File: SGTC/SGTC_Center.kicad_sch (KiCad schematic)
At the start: 0 parts

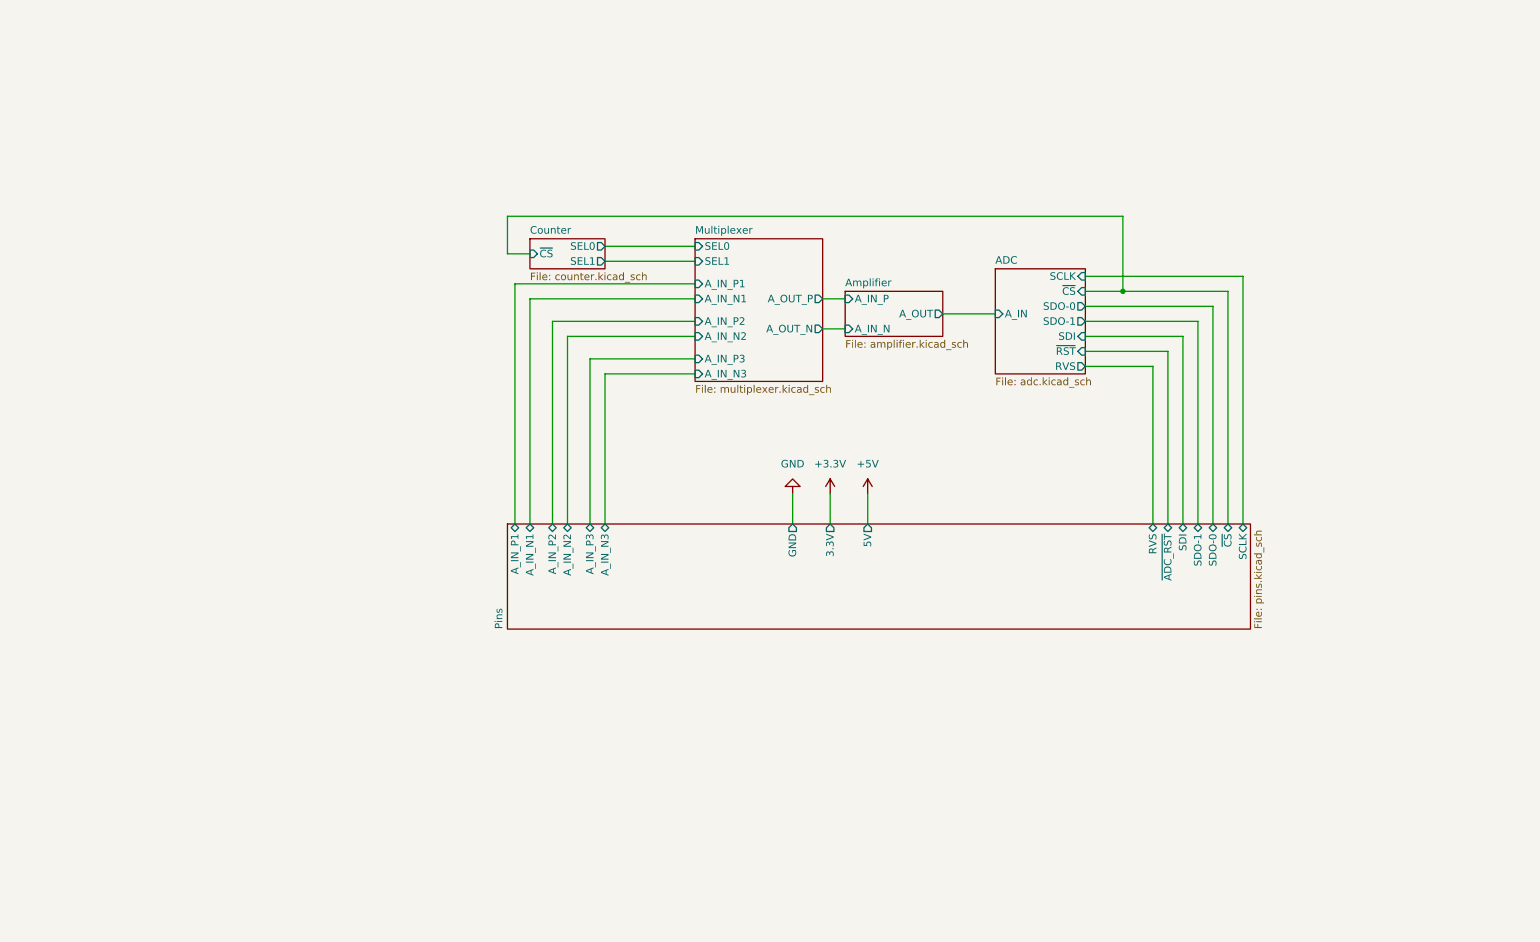
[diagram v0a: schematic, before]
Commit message: redo schematic for fin board
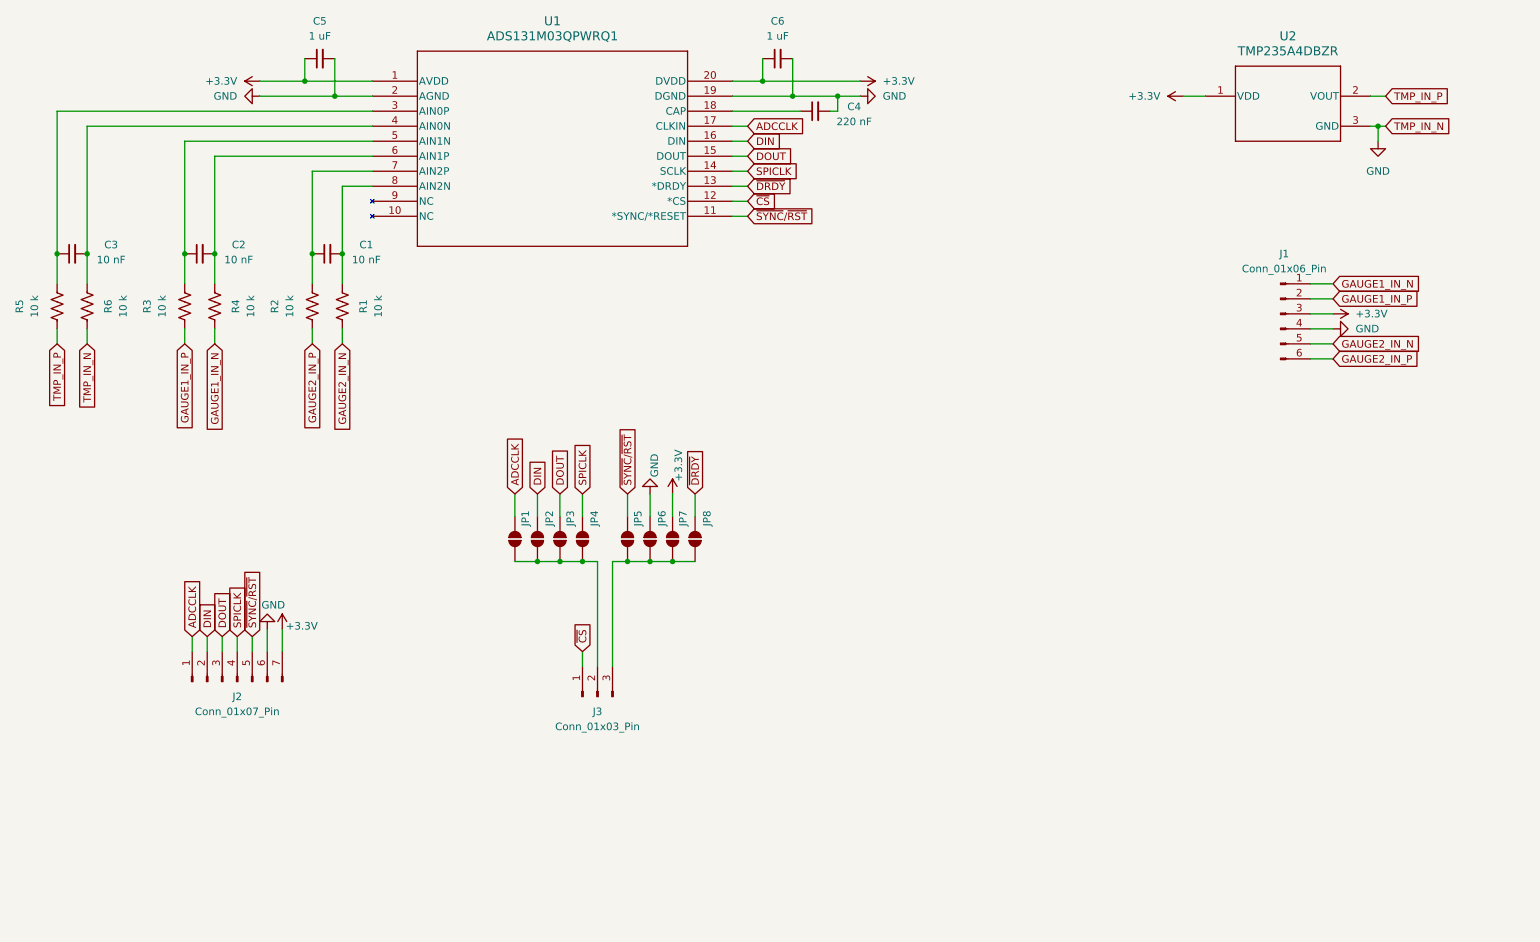
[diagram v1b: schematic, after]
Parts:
- added C1, C2, C3: 10 nF, symbol Device:C_Small
- added C4: 220 nF, symbol Device:C_Small
- added C5, C6: 1 uF, symbol Device:C_Small
- added J1: Conn_01x06_Pin, symbol Connector:Conn_01x06_Pin
- added J2: Conn_01x07_Pin, symbol Connector:Conn_01x07_Pin
- added J3: Conn_01x03_Pin, symbol Connector:Conn_01x03_Pin
- added JP1, JP2, JP3, JP4, JP5, JP6, JP7, JP8: SolderJumper_2_Open, symbol Jumper:SolderJumper_2_Open
- added R1, R2, R3, R4, R5, R6: 10 k, symbol Device:R_US
- added U1: ADS131M03QPWRQ1, TSSOP20_PW_TEX, symbol FinLib:ADS131M03QPWRQ1
- added U2: TMP235A4DBZR, DBZ0003A-IPC_A, symbol FinLib:TMP235A4DBZR
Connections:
- net +3.3V: now also C5.1, C6.1, J1.3 (Pin_3), J2.7 (Pin_7), JP7.2 (B), U1.1 (AVDD), U1.20 (DVDD), U2.1 (VDD)
- net GND: now also C4.2, C5.2, C6.2, J1.4 (Pin_4), J2.6 (Pin_6), JP6.2 (B), R6.2, U1.19 (DGND), U1.2 (AGND), U2.3 (GND)
- new net: J3.2 (Pin_2), JP1.1 (A), JP2.1 (A), JP3.1 (A), JP4.1 (A)
- new net: C1.1, R2.2, U1.7 (AIN2P)
- new net: C1.2, R1.1, U1.8 (AIN2N)
- new net: C3.1, R5.2, U1.3 (AIN0P)
- new net: C3.2, R6.1, U1.4 (AIN0N)
- new net: C2.1, R3.2, U1.5 (AIN1N)
- new net: C2.2, R4.1, U1.6 (AIN1P)
- new net: J3.3 (Pin_3), JP5.1 (A), JP6.1 (A), JP7.1 (A), JP8.1 (A)
- new net: C4.1, U1.18 (CAP)
- new net ADCCLK: J2.1 (Pin_1), JP1.2 (B), U1.17 (CLKIN)
- new net DIN: J2.2 (Pin_2), JP2.2 (B), U1.16 (DIN)
- new net DOUT: J2.3 (Pin_3), JP3.2 (B), U1.15 (DOUT)
- new net GAUGE1_IN_N: J1.1 (Pin_1), R4.2
- new net GAUGE1_IN_P: J1.2 (Pin_2), R3.1
- new net GAUGE2_IN_N: J1.5 (Pin_5), R1.2
- new net GAUGE2_IN_P: J1.6 (Pin_6), R2.1
- new net SPICLK: J2.4 (Pin_4), JP4.2 (B), U1.14 (SCLK)
- new net TMP_IN_P: R5.1, U2.2 (VOUT)
- new net ~{CS}: J3.1 (Pin_1), U1.12 (*CS)
- new net ~{DRDY}: JP8.2 (B), U1.13 (*DRDY)
- new net ~{SYNC}/~{RST}: J2.5 (Pin_5), JP5.2 (B), U1.11 (*SYNC/*RESET)
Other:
- removed sheet ADC
- removed sheet Amplifier
- removed sheet Counter
- removed sheet Multiplexer
- removed sheet Pins

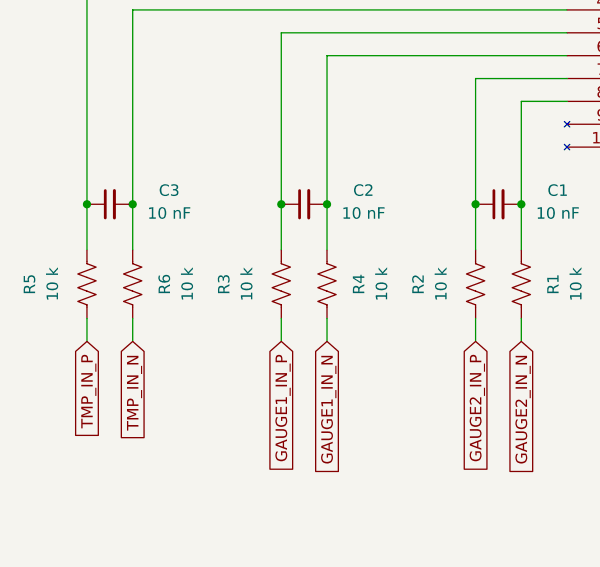
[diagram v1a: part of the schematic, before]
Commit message: fin center draft
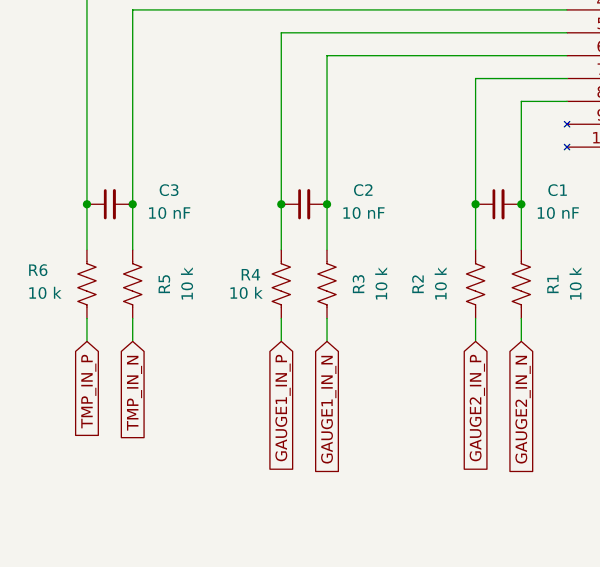
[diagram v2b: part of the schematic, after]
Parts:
- C1, C2, C3, C4, C5, C6: footprint (none) -> Capacitor_SMD:C_0603_1608Metric
- J1: footprint (none) -> Connector_PinHeader_2.54mm:PinHeader_1x06_P2.54mm_Vertical
- J2: footprint (none) -> Connector_PinHeader_2.54mm:PinHeader_1x07_P2.54mm_Vertical
- J3: footprint (none) -> Connector_PinHeader_2.54mm:PinHeader_1x03_P2.54mm_Vertical
- JP1, JP2, JP3, JP4, JP5, JP6, JP7, JP8: footprint (none) -> Jumper:SolderJumper-2_P1.3mm_Open_RoundedPad1.0x1.5mm
- R1, R2: footprint (none) -> Resistor_SMD:R_0603_1608Metric
- R3: renamed from R4; footprint (none) -> Resistor_SMD:R_0603_1608Metric
- R4: renamed from R3; footprint (none) -> Resistor_SMD:R_0603_1608Metric
- R5: renamed from R6; footprint (none) -> Resistor_SMD:R_0603_1608Metric
- R6: renamed from R5; footprint (none) -> Resistor_SMD:R_0603_1608Metric
- U1: footprint TSSOP20_PW_TEX -> FinLib:ADS131M03
- U2: footprint DBZ0003A-IPC_A -> FinLib:TMP235A4DBZR
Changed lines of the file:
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@@
 			)
 		)
-		(property "Footprint" ""
+		(property "Footprint" "Capacitor_SMD:C_0603_1608Metric"
 			(at 146.05 48.26 0)
 			(effects
@@
 			)
 		)
-		(property "Footprint" ""
+		(property "Footprint" "Jumper:SolderJumper-2_P1.3mm_Open_RoundedPad1.0x1.5mm"
 			(at 101.6 129.54 0)
 			(effects
@@
 			)
 		)
-		(property "Footprint" ""
+		(property "Footprint" "Jumper:SolderJumper-2_P1.3mm_Open_RoundedPad1.0x1.5mm"
 			(at 105.41 129.54 0)
 			(effects
@@
 			)
 		)
-		(property "Footprint" ""
+		(property "Footprint" "Jumper:SolderJumper-2_P1.3mm_Open_RoundedPad1.0x1.5mm"
 			(at 109.22 129.54 0)
 			(effects
@@
 			)
 		)
-		(property "Footprint" ""
+		(property "Footprint" "Capacitor_SMD:C_0603_1608Metric"
 			(at 69.85 81.28 0)
 			(effects
@@
 			)
 		)
-		(property "Footprint" ""
+		(property "Footprint" "Jumper:SolderJumper-2_P1.3mm_Open_RoundedPad1.0x1.5mm"
 			(at 113.03 129.54 0)
 			(effects
@@
 			)
 		)
-		(property "Footprint" ""
+		(property "Footprint" "Capacitor_SMD:C_0603_1608Metric"
 			(at 26.67 81.28 0)
 			(effects
@@
 			)
 		)
-		(property "Footprint" ""
+		(property "Footprint" "Capacitor_SMD:C_0603_1608Metric"
 			(at 48.26 81.28 0)
 			(effects
@@
 			)
 		)
-		(property "Footprint" "DBZ0003A-IPC_A"
+		(property "Footprint" "FinLib:TMP235A4DBZR"
 			(at 218.44 54.61 0)
 			(effects
@@
 			)
 		)
-		(property "Footprint" ""
+		(property "Footprint" "Connector_PinHeader_2.54mm:PinHeader_1x06_P2.54mm_Vertical"
 			(at 231.14 91.44 0)
 			(effects
@@
 			)
 		)
-		(property "Footprint" ""
+		(property "Footprint" "Resistor_SMD:R_0603_1608Metric"
 			(at 66.294 89.916 90)
 			(effects
@@
 		(on_board yes)
 		(dnp no)
-		(property "Reference" "R4"
+		(property "Reference" "R3"
 			(at 54.356 90.17 90)
 			(effects
@@
 			)
 		)
-		(property "Footprint" ""
+		(property "Footprint" "Resistor_SMD:R_0603_1608Metric"
 			(at 51.816 90.424 90)
 			(effects
@@
 			(project "SGTC_Center"
 				(path "/cbc99ef0-5fa7-4678-bd4c-c2c08fe588b6"
-					(reference "R4")
+					(reference "R3")
 					(unit 1)
 				)
@@
 		(on_board yes)
 		(dnp no)
-		(fields_autoplaced yes)
-		(property "Reference" "R3"
-			(at 39.37 90.17 90)
-			(effects
-				(font
-					(size 1.27 1.27)
-				)
+		(property "Reference" "R4"
+			(at 41.148 89.154 0)
+			(effects
+				(font
+					(size 1.27 1.27)
+				)
+				(justify right)
 			)
 		)
 		(property "Value" "10 k"
-			(at 41.91 90.17 90)
-			(effects
-				(font
-					(size 1.27 1.27)
-				)
-			)
-		)
-		(property "Footprint" ""
+			(at 39.878 91.186 0)
+			(effects
+				(font
+					(size 1.27 1.27)
+				)
+				(justify right)
+			)
+		)
+		(property "Footprint" "Resistor_SMD:R_0603_1608Metric"
 			(at 44.704 89.916 90)
 			(effects
@@
 			(project "SGTC_Center"
 				(path "/cbc99ef0-5fa7-4678-bd4c-c2c08fe588b6"
-					(reference "R3")
+					(reference "R4")
 					(unit 1)
 				)
@@
 			)
 		)
-		(property "Footprint" ""
+		(property "Footprint" "Capacitor_SMD:C_0603_1608Metric"
 			(at 68.58 48.26 0)
 			(effects
@@
 			)
 		)
-		(property "Footprint" ""
+		(property "Footprint" "Jumper:SolderJumper-2_P1.3mm_Open_RoundedPad1.0x1.5mm"
 			(at 128.27 129.54 0)
 			(effects
@@
 			)
 		)
-		(property "Footprint" ""
+		(property "Footprint" "Connector_PinHeader_2.54mm:PinHeader_1x03_P2.54mm_Vertical"
 			(at 115.57 156.21 0)
 			(effects
@@
 		(on_board yes)
 		(dnp no)
-		(property "Reference" "R6"
+		(property "Reference" "R5"
 			(at 32.766 90.17 90)
 			(effects
@@
 			)
 		)
-		(property "Footprint" ""
+		(property "Footprint" "Resistor_SMD:R_0603_1608Metric"
 			(at 30.226 90.424 90)
 			(effects
@@
 			(project "SGTC_Center"
 				(path "/cbc99ef0-5fa7-4678-bd4c-c2c08fe588b6"
-					(reference "R6")
+					(reference "R5")
 					(unit 1)
 				)
@@
 			)
 		)
-		(property "Footprint" ""
+		(property "Footprint" "Jumper:SolderJumper-2_P1.3mm_Open_RoundedPad1.0x1.5mm"
 			(at 132.08 129.54 0)
 			(effects
@@
 		(on_board yes)
 		(dnp no)
-		(fields_autoplaced yes)
-		(property "Reference" "R5"
-			(at 17.78 90.17 90)
-			(effects
-				(font
-					(size 1.27 1.27)
-				)
+		(property "Reference" "R6"
+			(at 17.526 88.646 0)
+			(effects
+				(font
+					(size 1.27 1.27)
+				)
+				(justify right)
 			)
 		)
 		(property "Value" "10 k"
-			(at 20.32 90.17 90)
-			(effects
-				(font
-					(size 1.27 1.27)
-				)
-			)
-		)
-		(property "Footprint" ""
+			(at 17.526 91.186 0)
+			(effects
+				(font
+					(size 1.27 1.27)
+				)
+				(justify right)
+			)
+		)
+		(property "Footprint" "Resistor_SMD:R_0603_1608Metric"
 			(at 23.114 89.916 90)
 			(effects
@@
 			(project "SGTC_Center"
 				(path "/cbc99ef0-5fa7-4678-bd4c-c2c08fe588b6"
-					(reference "R5")
+					(reference "R6")
 					(unit 1)
 				)
@@
 			)
 		)
-		(property "Footprint" ""
+		(property "Footprint" "Jumper:SolderJumper-2_P1.3mm_Open_RoundedPad1.0x1.5mm"
 			(at 120.65 129.54 0)
 			(effects
@@
 			)
 		)
-		(property "Footprint" ""
+		(property "Footprint" "Resistor_SMD:R_0603_1608Metric"
 			(at 73.406 90.424 90)
 			(effects
@@
 			)
 		)
-		(property "Footprint" "TSSOP20_PW_TEX"
+		(property "Footprint" "FinLib:ADS131M03"
 			(at 77.47 52.07 0)
 			(effects
@@
 			)
 		)
-		(property "Footprint" ""
+		(property "Footprint" "Connector_PinHeader_2.54mm:PinHeader_1x07_P2.54mm_Vertical"
 			(at 54.61 153.67 0)
 			(effects
@@
 			)
 		)
-		(property "Footprint" ""
+		(property "Footprint" "Capacitor_SMD:C_0603_1608Metric"
 			(at 152.4 57.15 0)
 			(effects
@@
 			)
 		)
-		(property "Footprint" ""
+		(property "Footprint" "Jumper:SolderJumper-2_P1.3mm_Open_RoundedPad1.0x1.5mm"
 			(at 124.46 129.54 0)
 			(effects

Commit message: silkscreen things mostly
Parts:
- C1, C2, C3, C4, C5, C6: footprint Capacitor_SMD:C_0603_1608Metric -> (none)
- J1: footprint Connector_PinHeader_2.54mm:PinHeader_1x06_P2.54mm_Vertical -> (none)
- J2: footprint Connector_PinHeader_2.54mm:PinHeader_1x07_P2.54mm_Vertical -> (none)
- J3: footprint Connector_PinHeader_2.54mm:PinHeader_1x03_P2.54mm_Vertical -> (none)
- JP1, JP2, JP3, JP4, JP5, JP6, JP7, JP8: footprint Jumper:SolderJumper-2_P1.3mm_Open_RoundedPad1.0x1.5mm -> (none)
- R1, R2: footprint Resistor_SMD:R_0603_1608Metric -> (none)
- R3: renamed from R4; footprint Resistor_SMD:R_0603_1608Metric -> (none)
- R4: renamed from R3; footprint Resistor_SMD:R_0603_1608Metric -> (none)
- R5: renamed from R6; footprint Resistor_SMD:R_0603_1608Metric -> (none)
- R6: renamed from R5; footprint Resistor_SMD:R_0603_1608Metric -> (none)
- U1: footprint FinLib:ADS131M03 -> TSSOP20_PW_TEX
- U2: footprint FinLib:TMP235A4DBZR -> DBZ0003A-IPC_A
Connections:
- net at JP1.1 (A), JP2.1 (A), JP3.1 (A)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: now also J3.3 (Pin_3); no longer J3.2 (Pin_2)
- net at JP5.1 (A), JP6.1 (A), JP7.1 (A)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: now also J3.2 (Pin_2); no longer J3.3 (Pin_3)
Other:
- moved on the sheet: JP1, JP2, JP3, JP4, JP5, JP6, JP7, JP8

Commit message: final version
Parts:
- removed J2: Conn_01x07_Pin, symbol Connector:Conn_01x07_Pin
- added J2, J4, J5, J6, J7, J8, J9: Conn_01x01_Pin, Connector_PinHeader_2.54mm:PinHeader_1x01_P2.54mm_Vertical, symbol Connector:Conn_01x01_Pin
- C1, C2, C3, C4, C5, C6: footprint (none) -> Capacitor_SMD:C_0603_1608Metric
- J1: footprint (none) -> Connector_PinHeader_2.54mm:PinHeader_1x06_P2.54mm_Vertical
- J3: footprint (none) -> Connector_PinHeader_2.54mm:PinHeader_1x03_P2.54mm_Vertical
- JP1, JP2, JP3, JP4, JP5, JP6, JP7, JP8: footprint (none) -> Jumper:SolderJumper-2_P1.3mm_Open_RoundedPad1.0x1.5mm
- R1, R2, R3, R4, R5, R6: footprint (none) -> Resistor_SMD:R_0603_1608Metric
- U1: footprint TSSOP20_PW_TEX -> FinLib:ADS131M03
- U2: footprint DBZ0003A-IPC_A -> FinLib:TMP235A4DBZR
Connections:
- net +3.3V: now also J9.1 (Pin_1)
- net ADCCLK: now also J2.1 (Pin_1)
- net DIN: now also J4.1 (Pin_1)
- net DOUT: now also J5.1 (Pin_1)
- net GND: now also J8.1 (Pin_1)
- net SPICLK: now also J6.1 (Pin_1)
- net ~{SYNC}/~{RST}: now also J7.1 (Pin_1)

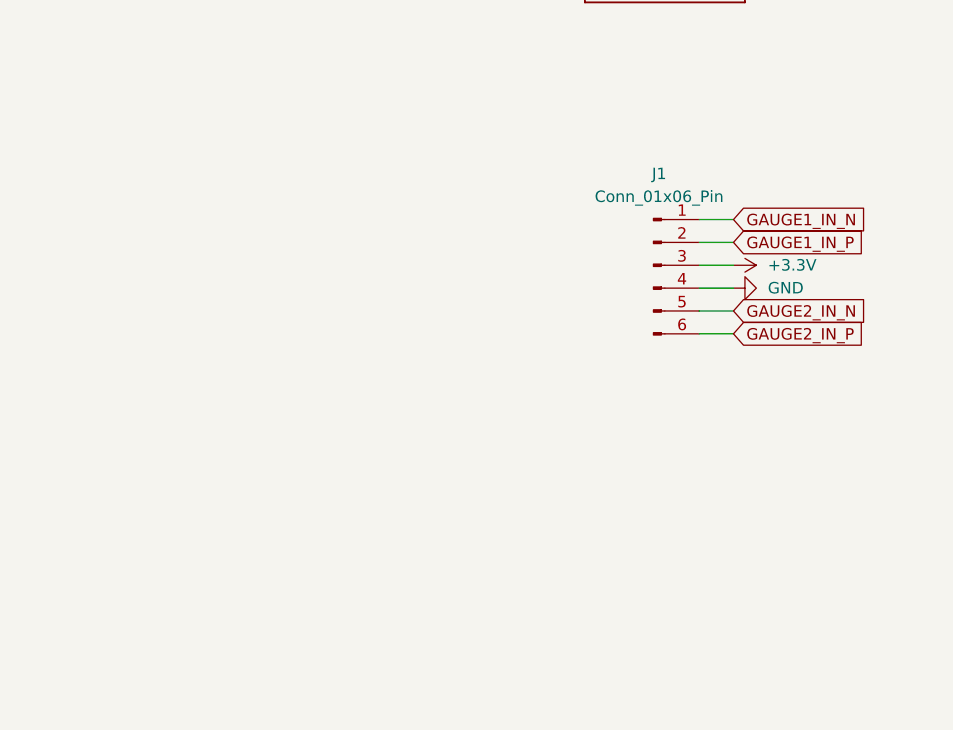
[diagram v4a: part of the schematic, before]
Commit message: fixed core dimensions and pin locations
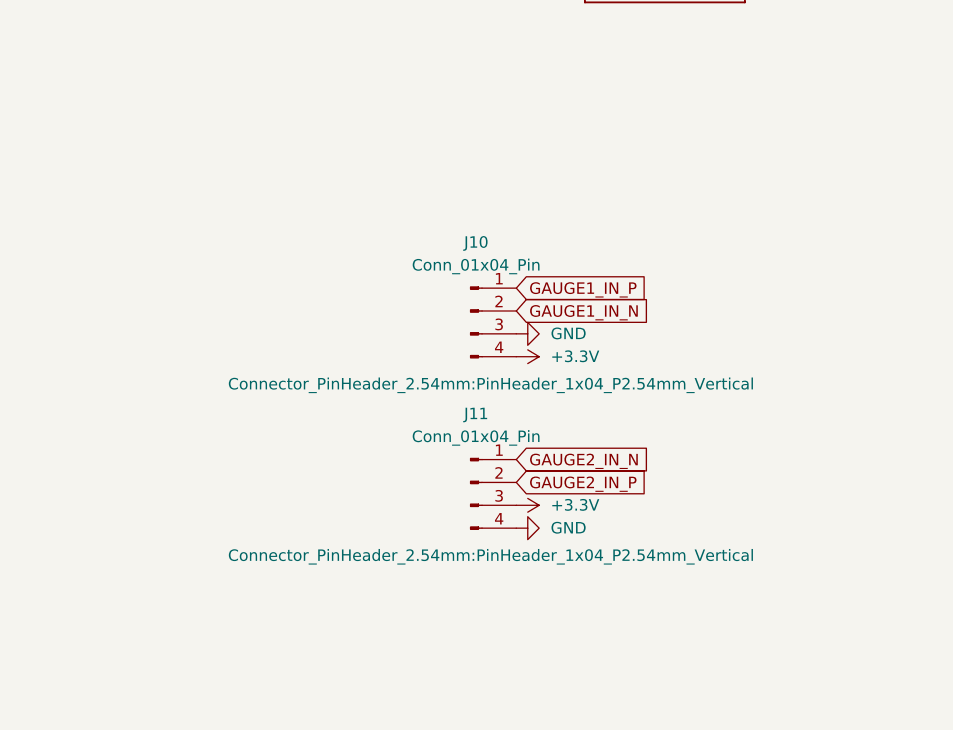
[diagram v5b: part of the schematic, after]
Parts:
- removed J1: Conn_01x06_Pin, Connector_PinHeader_2.54mm:PinHeader_1x06_P2.54mm_Vertical, symbol Connector:Conn_01x06_Pin
- added J10, J11: Conn_01x04_Pin, Connector_PinHeader_2.54mm:PinHeader_1x04_P2.54mm_Vertical, symbol Connector:Conn_01x04_Pin
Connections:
- net +3.3V: now also J10.4 (Pin_4), J11.3 (Pin_3)
- net GAUGE1_IN_N: now also J10.2 (Pin_2)
- net GAUGE1_IN_P: now also J10.1 (Pin_1)
- net GAUGE2_IN_N: now also J11.1 (Pin_1)
- net GAUGE2_IN_P: now also J11.2 (Pin_2)
- net GND: now also J10.3 (Pin_3), J11.4 (Pin_4)
